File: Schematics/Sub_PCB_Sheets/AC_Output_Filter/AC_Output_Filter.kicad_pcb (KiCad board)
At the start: 2 copper layers, 93 x 90.5 mm, 14 parts, among them J17 464379202, J3 CONN_66.9040-21_MTC, J4 CONN_66.9040-21_MTC

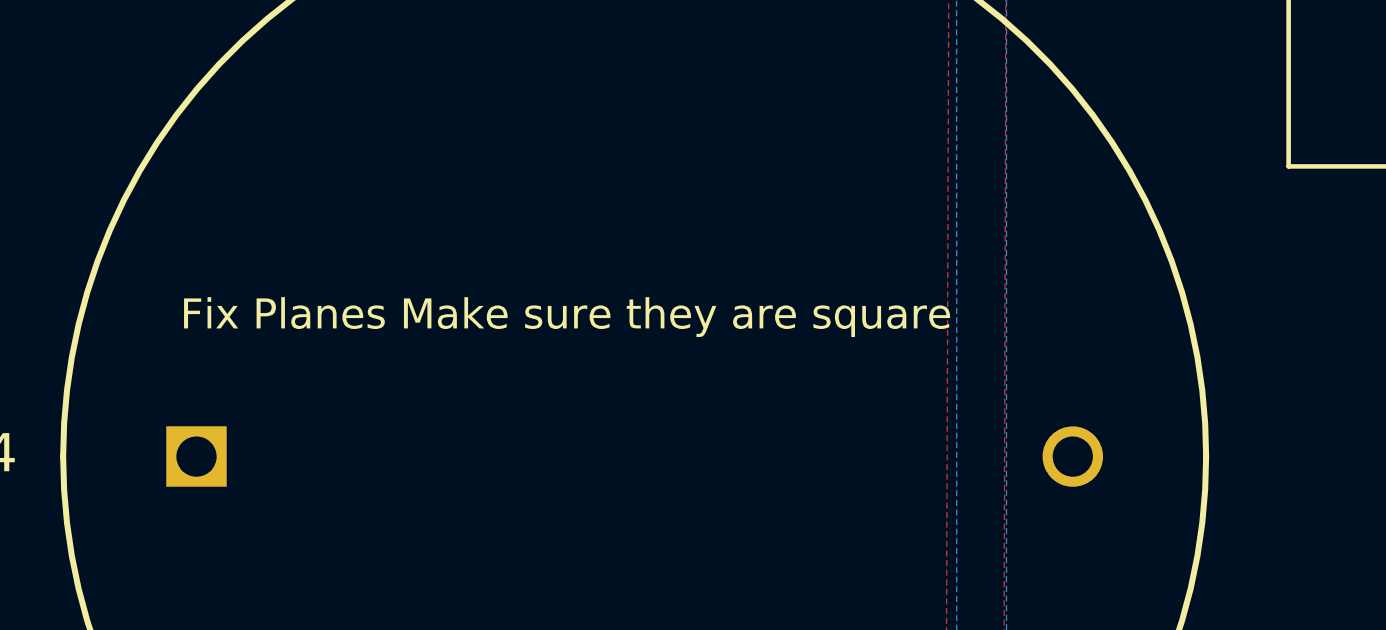
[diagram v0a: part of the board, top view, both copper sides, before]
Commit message: updated controller PCB to 4 layer and finished PCB tracing
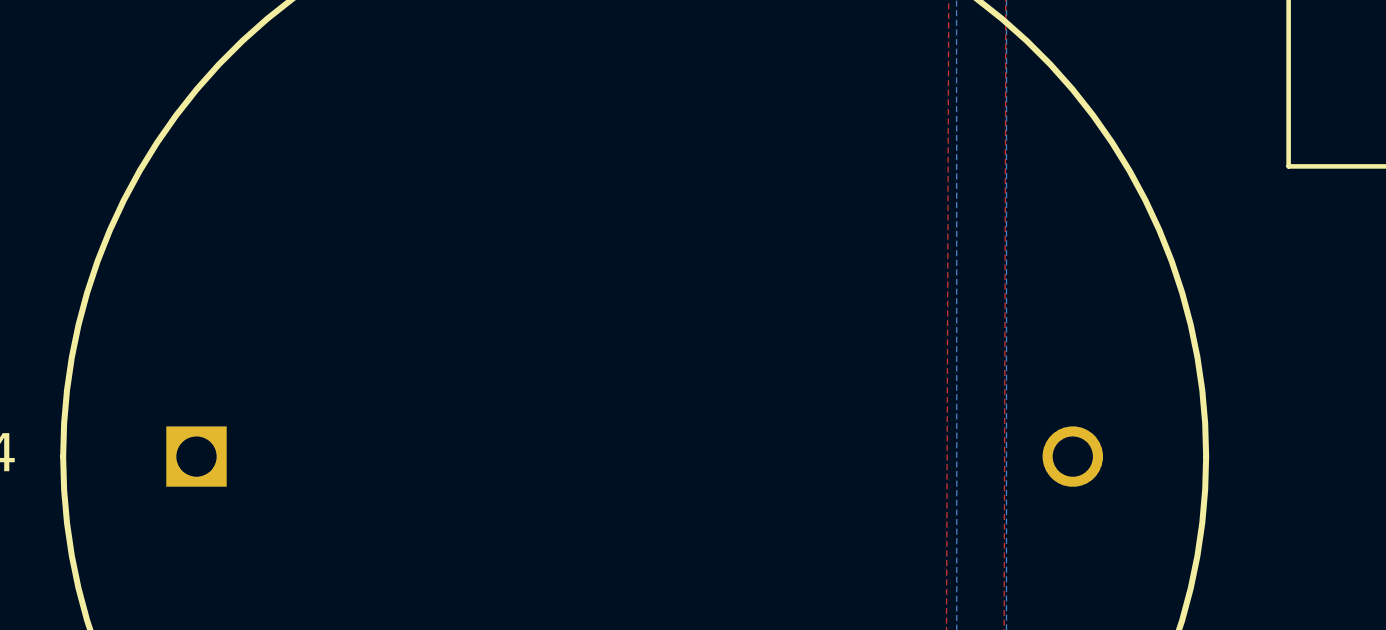
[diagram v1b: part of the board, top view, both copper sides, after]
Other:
- board text removed: "Fix Planes Make sure they are square"
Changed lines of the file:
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@@
-		)
-	)
-	(gr_text "Fix Planes Make sure they are square"
-		(at 124.95 83.55 0)
-		(layer "F.SilkS")
-		(effects
-			(font
-				(size 1 1)
-				(thickness 0.15)
-			)
-			(justify left bottom)
 		)
 	)
